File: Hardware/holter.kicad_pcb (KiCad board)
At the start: 6 copper layers, 33.5 x 48 mm, 262 parts, among them CN1 2TAP, CN2 2TAP, CN3 3TAP, IC1 256kx8, M1 USB_Power_Module, M2 USB_Power_Module, P1 CONN_01X07, P2 PROG, P3 SCREW, P4 BAT-, Q1 PMF170XP, Q2 PMF170XP, Q3 NTR4101PT1G, Q4 PMF170XP, Q5 PMF170XP, U1 TXB0106, U10 TS5A3159, U11 TS5A3159, U12 ESD_PROTECTOR, U13 ESD_PROTECTOR, U14 ESD_PROTECTOR, U15 ESD_PROTECTOR, U16 ESD_PROTECTOR, U17 ESD_PROTECTOR, U18 ESD_PROTECTOR, U19 ESD_PROTECTOR, U2 TXB0106, U20 ESD_PROTECTOR, U21 ESD_PROTECTOR, U22 ESD_PROTECTOR, U23 ESD_PROTECTOR, U24 TLV61220, U25 TLV61220, U26 TLV61220, U27 LM3671, U28 DS2710, U29 LIS2DH12, U3 TiWi-uB2, U4 STM32F4x1_64, U5 uSD, U6 ADS1298, U7 USBULC6-2M6, U8 USB2641, U9 OPA379, X1 32768, Y1 24 MHz, Y2 10 MHz

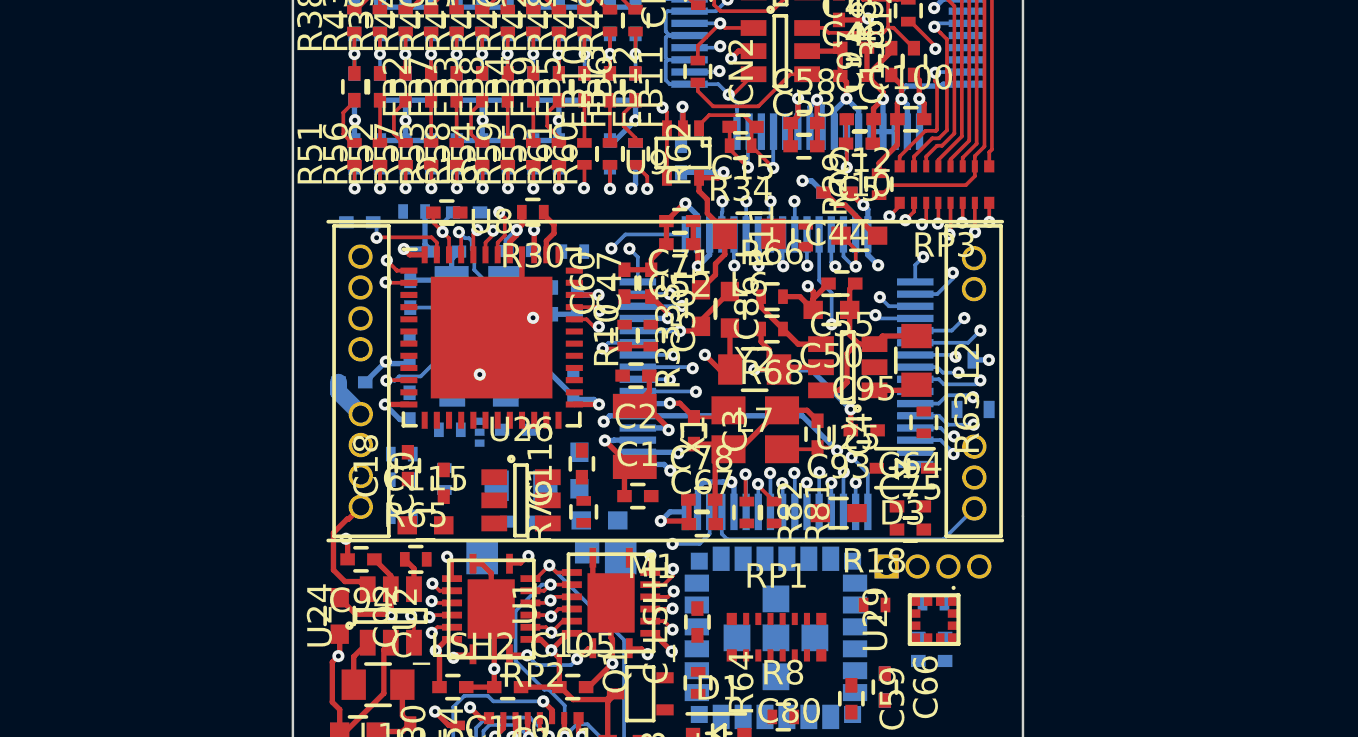
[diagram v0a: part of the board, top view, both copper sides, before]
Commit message: Moved the card reader to the other side. More routes.
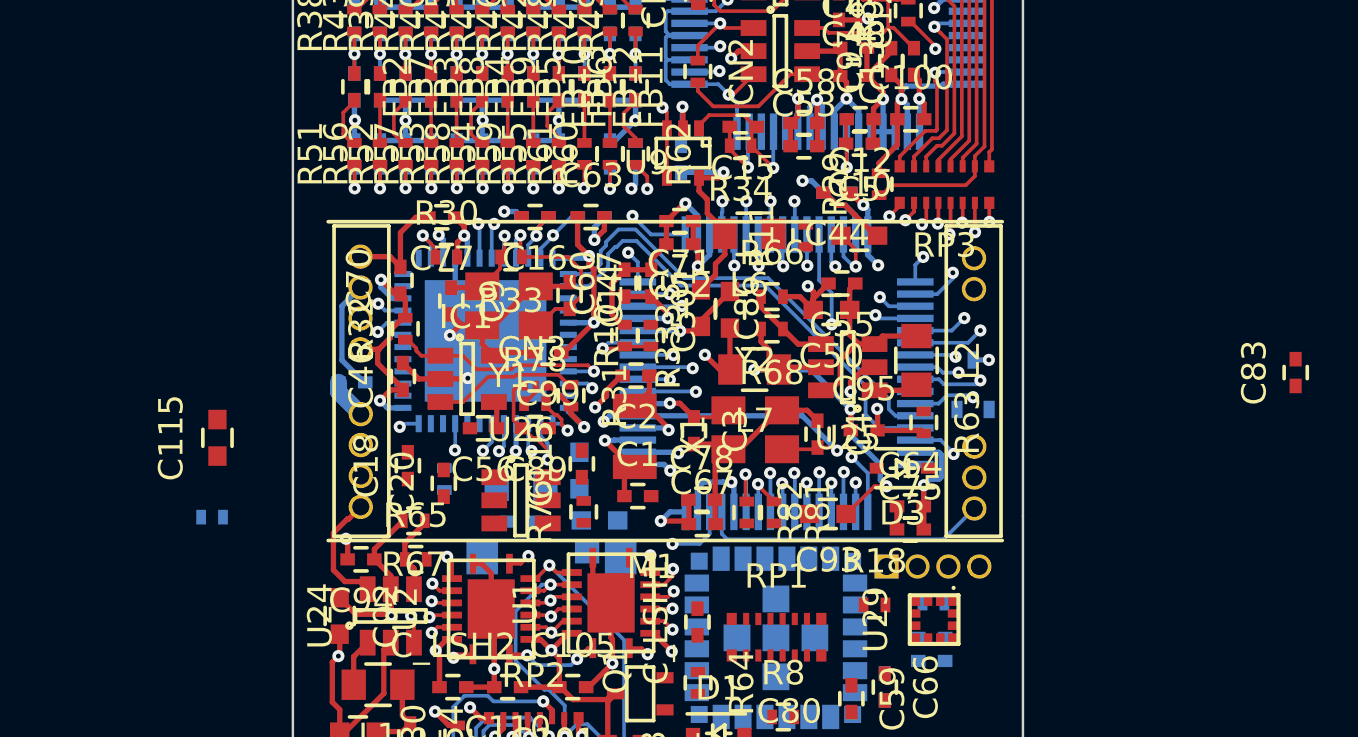
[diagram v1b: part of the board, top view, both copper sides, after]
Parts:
- C14, C46, C56, C63, C70, C77, C83, C89, C9, C99, CN3, IC1, R31, R32, R33, R67, R78, Y1: moved to F.Cu
- U8: moved to B.Cu
- moved C83 29.7 mm to (116.2, 59.1)
- moved R31 9.95 mm to (86.4, 60.0), turned to 270 degrees
- moved R35 9.51 mm to (87.3, 52.7), turned to 0 degrees
- moved C115 9.28 mm to (71.9, 61.8), turned to 90 degrees
- moved R36 7.95 mm to (71.7, 65.0)
- moved C70 7.30 mm to (79.4, 55.3), turned to 90 degrees
- moved C63 6.14 mm to (87.2, 52.7)
- moved C99 5.68 mm to (85.5, 58.3), turned to 180 degrees
- moved C46 5.61 mm to (79.5, 59.3), turned to 90 degrees
- moved C89 5.24 mm to (85.0, 61.4), turned to 180 degrees
- moved R32 5.15 mm to (79.6, 57.3), turned to 90 degrees
- moved R30 4.00 mm to (81.3, 54.4), turned to 0 degrees
- moved R78 3.66 mm to (85.0, 60.4), turned to 0 degrees
- moved C16 3.63 mm to (85.0, 52.7), turned to 180 degrees
- moved C77 3.49 mm to (81.1, 52.7), turned to 180 degrees
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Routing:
- net GND: track 165.8 -> 198.3 mm, vias 41 -> 46
- net (no net): track 30.0 -> 50.6 mm
- net DP: track 18.4 -> 1.43 mm
- net DM: track 18.3 -> 1.45 mm
- net MCU_USB_DP: track 2.70 -> 19.2 mm, vias 2 -> 0
- net MCU_USB_DM: track 3.64 -> 18.8 mm, vias 2 -> 0
- net +3V3: track 37.1 -> 48.1 mm, vias 7 -> 9
- net Net-(IC1-Pad1): track 0.00 -> 9.53 mm, vias 0 -> 1
- net Net-(C93-Pad1): track 10.3 -> 16.2 mm, vias 2 -> 3
- net Net-(C14-Pad2): track 4.32 -> 8.05 mm
- net Net-(IC1-Pad3): track 4.12 -> 7.06 mm
- net Net-(R78-Pad2): track 0.00 -> 2.26 mm, vias 0 -> 1
- net +2.8VD: track 17.2 -> 19.2 mm
- net Net-(R65-Pad1): track 1.38 -> 3.30 mm
- net Net-(C9-Pad1): track 2.98 -> 4.68 mm
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
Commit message: More traces.
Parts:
- added C_ADC1: 100nF, Capacitors_SMD:C_0402, B.Cu at (103.1, 48.9)
- C111, R75: moved to F.Cu
- C113, C115: moved to B.Cu
- moved C115 26.4 mm to (82.2, 37.5), turned to 270 degrees
- moved R36 13.0 mm to (84.6, 63.3)
- moved C128 7.11 mm to (80.5, 64.3), turned to 90 degrees
- moved C18 6.44 mm to (86.2, 63.0), turned to 270 degrees
- moved R76 6.39 mm to (80.7, 63.7), turned to 270 degrees
- moved C20 5.97 mm to (87.1, 63.0), turned to 270 degrees
- moved C131 5.27 mm to (79.2, 64.5), turned to 90 degrees
- moved C83 3.05 mm to (114.5, 61.6), turned to 270 degrees
- moved C113 2.28 mm to (86.5, 65.1), turned to 0 degrees
- moved C111 1.98 mm to (86.6, 65.1), turned to 0 degrees
- moved R75 1.60 mm to (79.6, 63.7)
- moved L3 1.55 mm to (83.2, 64.7), turned to 0 degrees
- moved U26 1.21 mm to (83.2, 64.2), turned to 180 degrees
- moved C56 0.06 mm to (82.8, 61.3)
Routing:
- net +3V3: track 48.1 -> 100.1 mm
- net Net-(C128-Pad1): track 0.00 -> 28.9 mm, vias 0 -> 2
- net Net-(M1-Pad3): track 0.00 -> 24.5 mm
- net GND: track 198.3 -> 221.3 mm, vias 46 -> 49
- net (no net): track 50.6 -> 30.0 mm
- net DP: track 1.43 -> 18.5 mm
- net DM: track 1.45 -> 18.4 mm
- net BAT+: track 35.6 -> 51.2 mm, vias 3 -> 5
- net CR_D3: track 2.15 -> 17.5 mm
- net CR_D2: track 1.99 -> 15.1 mm
- net CR_CMD: track 1.76 -> 13.2 mm
- net CR_CLK: track 1.95 -> 11.4 mm
- net EN_2V8: track 1.15 -> 9.62 mm, vias 1 -> 2
- net CR_D1: track 2.14 -> 9.48 mm
- net CR_D0: track 2.24 -> 7.21 mm
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
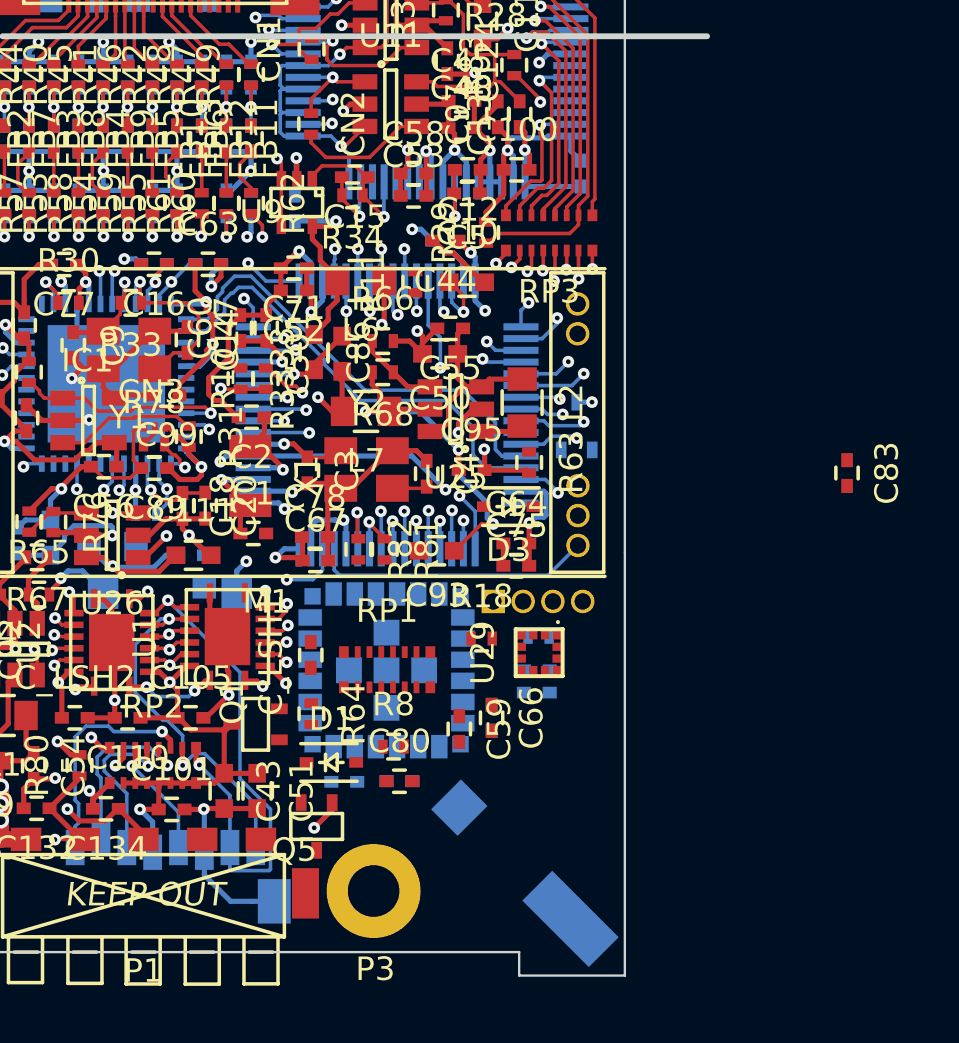
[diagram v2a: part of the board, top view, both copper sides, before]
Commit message: Rearrangement of CPU pins, even more traces, fixed LGA footprint
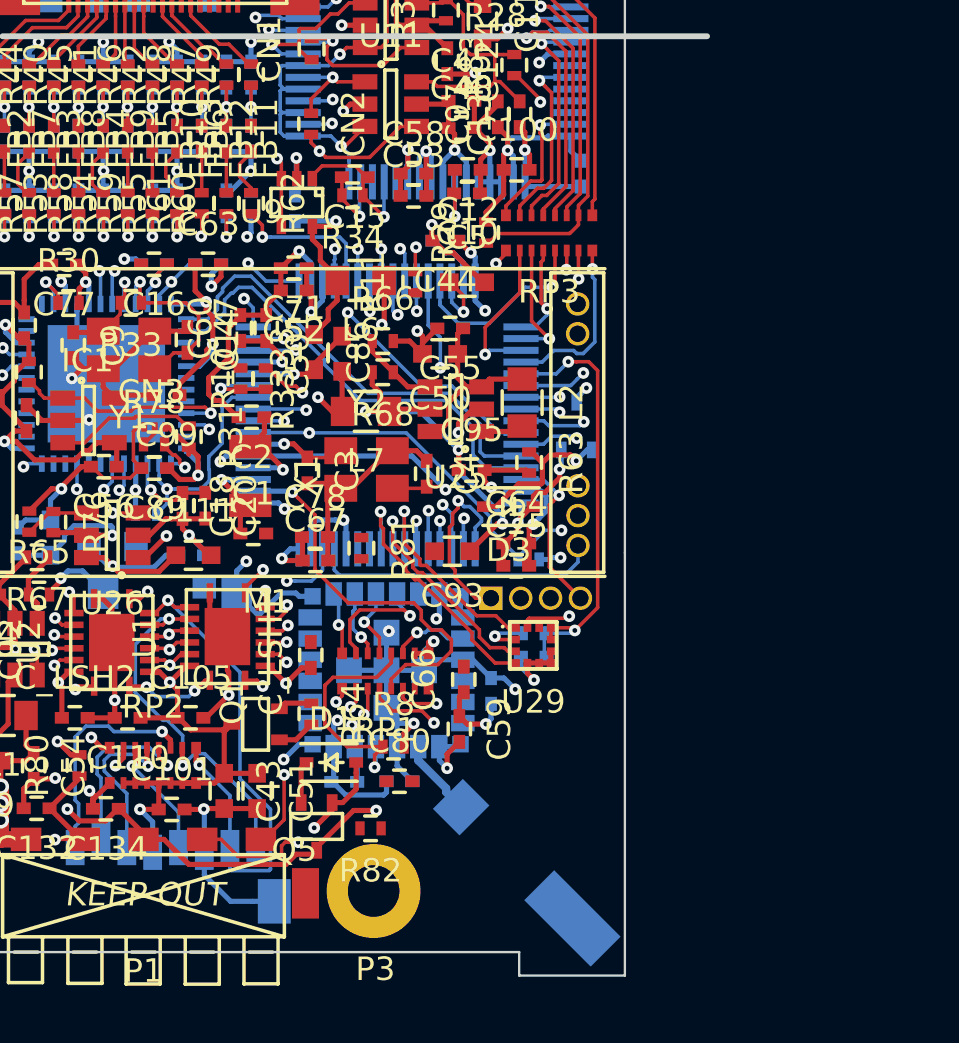
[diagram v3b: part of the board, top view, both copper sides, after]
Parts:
- removed C138: 1uF, Capacitors_SMD:C_0402
- removed C83: 100nF, Capacitors_SMD:C_0402
- R18: moved to B.Cu
- moved R82 11.9 mm to (94.2, 76.7), turned to 180 degrees
- moved R18 3.92 mm to (100.9, 65.3), turned to 180 degrees
- moved C66 2.02 mm to (98.1, 70.4), turned to 90 degrees
- moved C74 1.15 mm to (99.3, 70.9), turned to 90 degrees
- moved R81 1.00 mm to (93.8, 64.8)
- moved C93 0.67 mm to (97.7, 64.9)
- moved C139 0.59 mm to (101.1, 69.4)
- moved U29 0.40 mm to (101.1, 68.9), turned to 0 degrees
- moved R85 0.26 mm to (101.1, 68.4), turned to 0 degrees
- moved P2 0.17 mm to (101.5, 67.1)
- moved RP1 0.09 mm to (94.8, 70.0), turned to 0 degrees
- moved ANT1 0.08 mm to (100.7, 78.5)
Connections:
- R85 pad 2: GND -> ACC_PWR
- U4 pad 10: CABLE_DETECT -> ~CARD_DET
- U4 pad 21: ECG_START -> CABLE_DETECT
- U4 pad 29: ~CARD_DET -> ECG_START
- U4 pad 33: ACC_CS -> ~ECG_CS
- U4 pad 34: ACC_CLK -> SPI_SCK
- U4 pad 35: ACC_MISO -> SPI_MISO
- U4 pad 36: ACC_MOSI -> SPI_MOSI
- U4 pad 50: ~ECG_CS -> ACC_CS
- U4 pad 55: SPI_SCK -> ACC_CLK
- U4 pad 56: SPI_MISO -> ACC_MISO
- U4 pad 57: SPI_MOSI -> ACC_MOSI
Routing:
- net GND: track 221.3 -> 258.7 mm, vias 49 -> 58
- net RX: track 2.48 -> 32.7 mm, vias 1 -> 2
- net SD_CPU: track 4.87 -> 34.0 mm, vias 2 -> 3
- net TX: track 1.37 -> 26.9 mm, vias 1 -> 2
- net +2.8VD: track 19.2 -> 44.5 mm, vias 2 -> 4
- net +5V: track 27.5 -> 50.4 mm, vias 1 -> 2
- net +1V8: track 64.4 -> 85.4 mm, vias 6 -> 7
- net CTS: track 1.82 -> 21.3 mm, vias 1 -> 2
- net RTS: track 1.31 -> 20.4 mm, vias 1 -> 2
- net 32768_CLK: track 2.83 -> 21.9 mm, vias 1 -> 2
- net CR_SEL: track 11.1 -> 29.1 mm
- net BTN: track 7.82 -> 25.5 mm
- net ~RST: track 2.39 -> 20.0 mm, vias 1 -> 2
- net ACC_PWR: track 2.23 -> 19.1 mm, vias 1 -> 2
- net SDIO_D0: track 2.39 -> 18.7 mm
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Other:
- net class 50 Ohm added: clearance 0.1524, trace_width 0.347, via_dia 0.5, via_drill 0.2

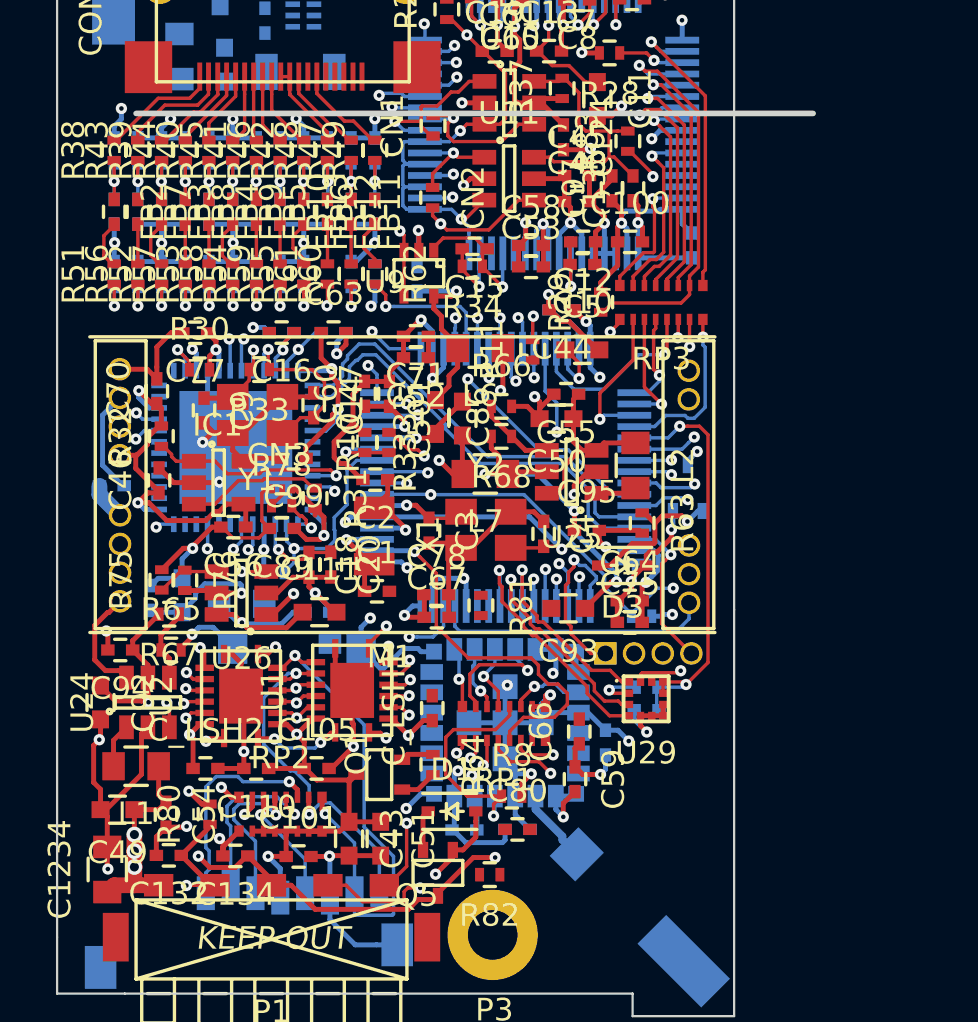
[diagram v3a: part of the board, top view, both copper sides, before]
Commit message: Pin rearrangement, more traces.
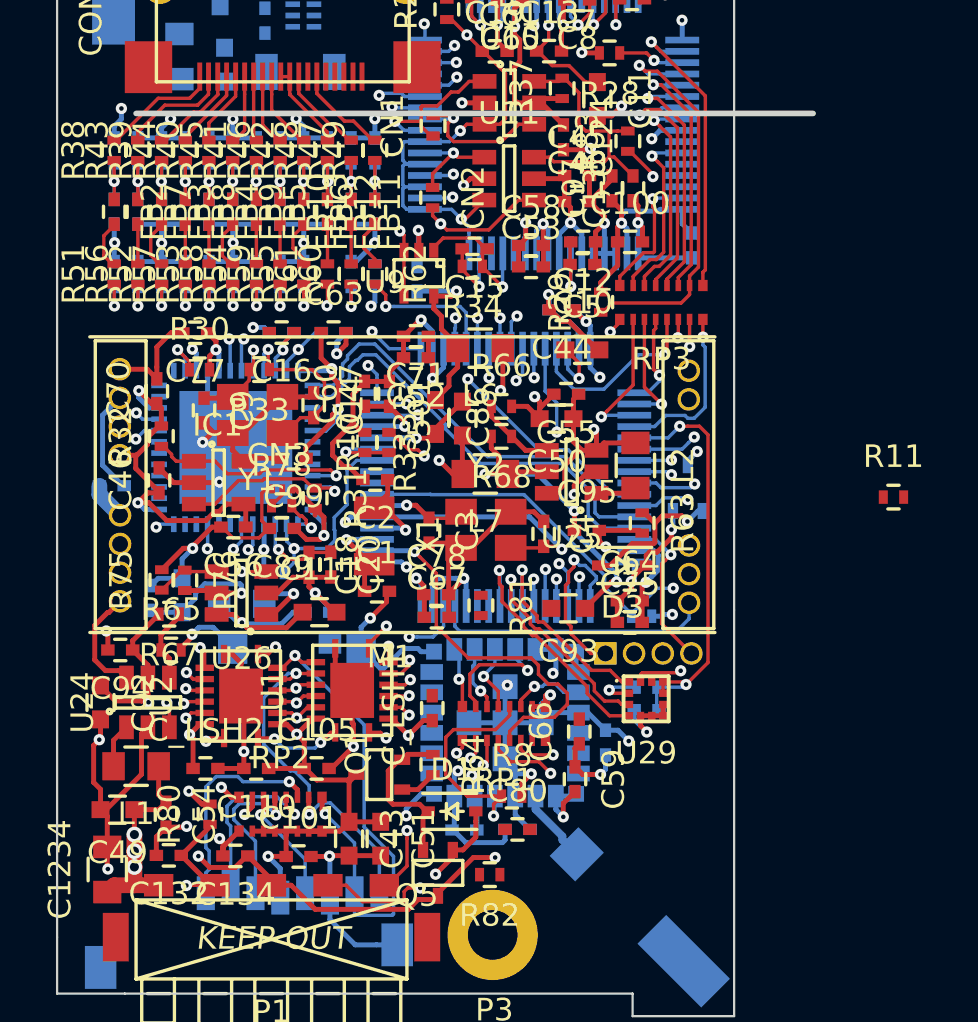
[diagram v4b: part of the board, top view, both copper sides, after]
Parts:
- moved R11 17.3 mm to (112.1, 60.0), turned to 0 degrees
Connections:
- M1 pad 10: +2.8VD -> ~CHRG_EN
- M1 pad 11: ~CHRG_STAT -> VBAT
- M1 pad 12: ~CHRG_EN -> +2.8VD
- M1 pad 9: VBAT -> ~CHRG_STAT
- M2 pad 10: Net-(D4-Pad2) -> /Power/USB Power/~CHRG_EN
- M2 pad 11: /Power/USB Power/~CHRG_STAT -> Net-(C62-Pad1)
- M2 pad 12: /Power/USB Power/~CHRG_EN -> Net-(D4-Pad2)
- M2 pad 9: Net-(C62-Pad1) -> /Power/USB Power/~CHRG_STAT
- U4 pad 25: Net-(R11-Pad1) -> ~CHRG_STAT
- U4 pad 26: ~SD_EN -> ~CHRG_EN
- U4 pad 8: ~CHRG_EN -> ~SD_EN
- U4 pad 9: ~CHRG_STAT -> Net-(R11-Pad1)
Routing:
- net SDIO_CLK: track 2.49 -> 14.8 mm
- net ~CHRG_EN: track 1.32 -> 10.4 mm
- net BAT+: track 51.2 -> 60.2 mm, vias 5 -> 6
- net ~CHRG_STAT: track 2.27 -> 10.7 mm
- net GND: track 258.7 -> 263.4 mm
- net Net-(D1-Pad1): track 3.26 -> 7.34 mm
- net SDIO_D3: track 16.1 -> 19.0 mm
- net Net-(R11-Pad1): track 1.58 -> 0.00 mm, vias 1 -> 0
- net Net-(L3-Pad2): track 1.59 -> 3.08 mm
- net ~SD_EN: track 3.09 -> 1.63 mm, vias 1 -> 0
- net EN_2V8: track 10.7 -> 9.62 mm, vias 3 -> 2
- net Net-(IC1-Pad3): track 7.06 -> 7.99 mm
- net Net-(C32-Pad1): track 2.56 -> 3.37 mm
- net Net-(C30-Pad1): track 2.55 -> 3.35 mm
- net Net-(C29-Pad1): track 2.55 -> 3.35 mm
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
